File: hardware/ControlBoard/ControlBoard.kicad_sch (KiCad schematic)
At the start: 157 parts, among them J1 Lamp 1 Out, J10 CAN, J11 USB_B_Micro, J12 Conn_01x02, J13 AVAILABLE GPIO, J14 MOTOR_CTRL1, J15 MOTOR_CTRL2, J2 ESTOP1, J3 ESTOP2, J4 Lamp 3 Out, J5 Lamp 2 Out, J6 Lamp 4 Out, J7 PWR_IN, J8 USB_B_Micro, J9 UART BACKUP, Q1 DMN62D0U-13, Q2 DMN62D0U-13, Q3 DMN62D0U-13, Q4 DMN62D0U-13, Q5 SS8050-G, Q6 SS8050-G, SW1 SW_Push, SW2 SW_Push, U1 CP2102N-A02-GQFN28, U2 Lora_Module, U3 AZ1117IH-5.0TRG1, U4 LD1086DT33TR, U5 ESP32-S3-WROOM-1U-N16, U6 74LVC1G97W6-7, U7 SN65HVD232, U8 SN74LVC1GU04DBVR

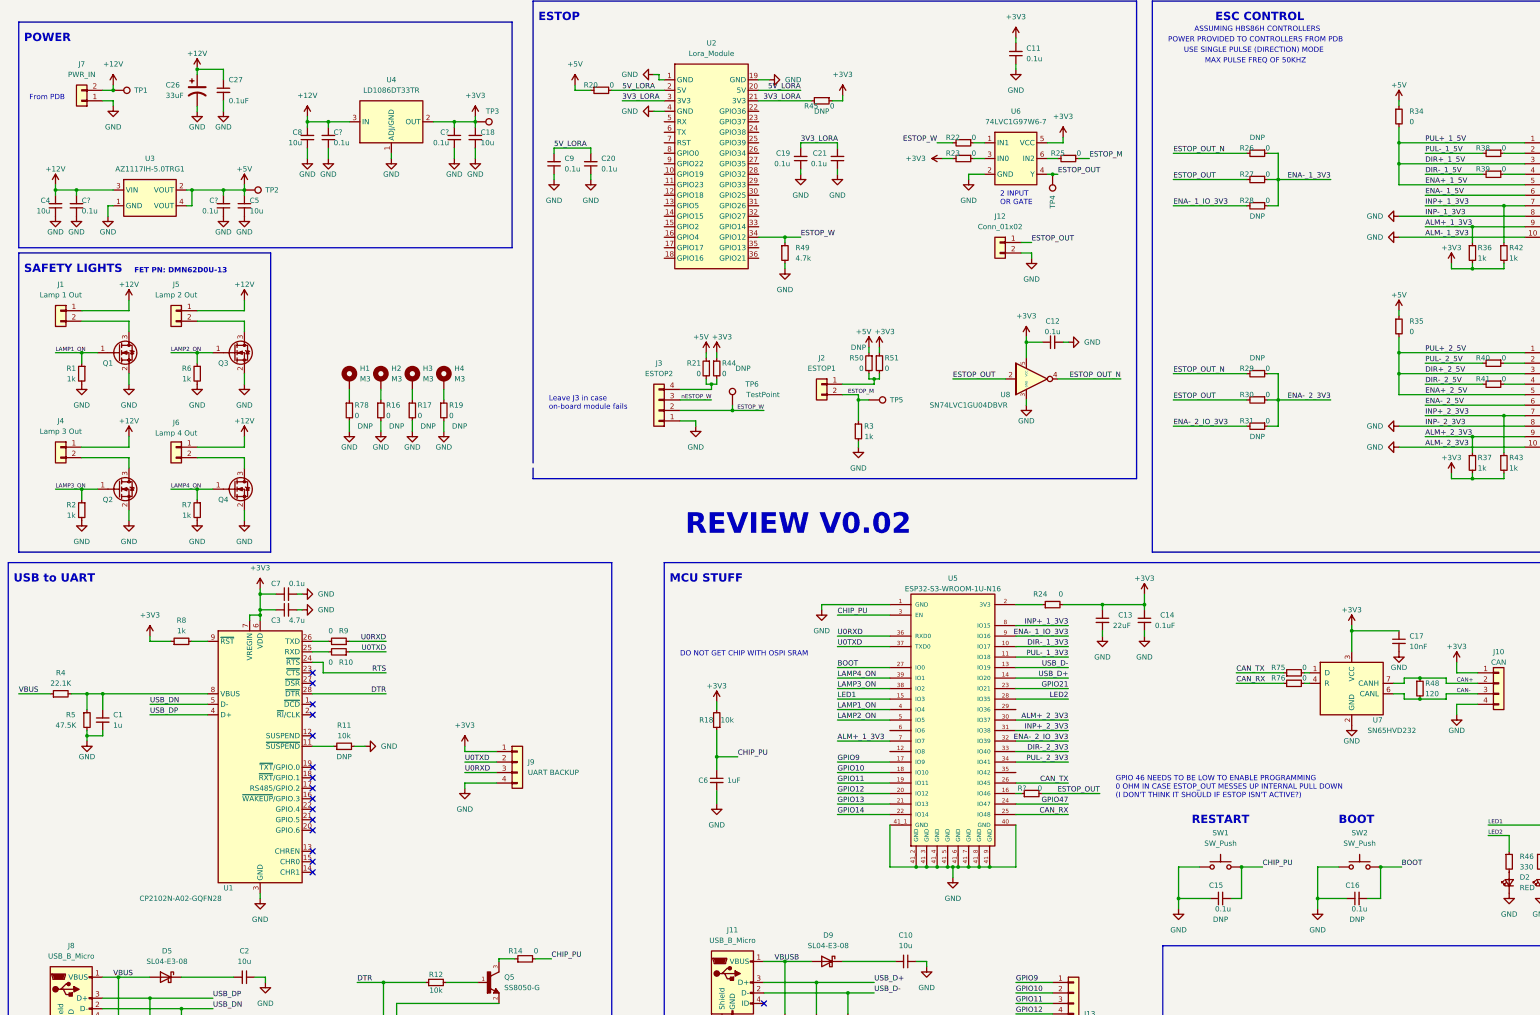
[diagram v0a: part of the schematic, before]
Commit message: Control Board - Replace LDOs, Fix ESP Strapping Pins, W EStop Voltage Divider
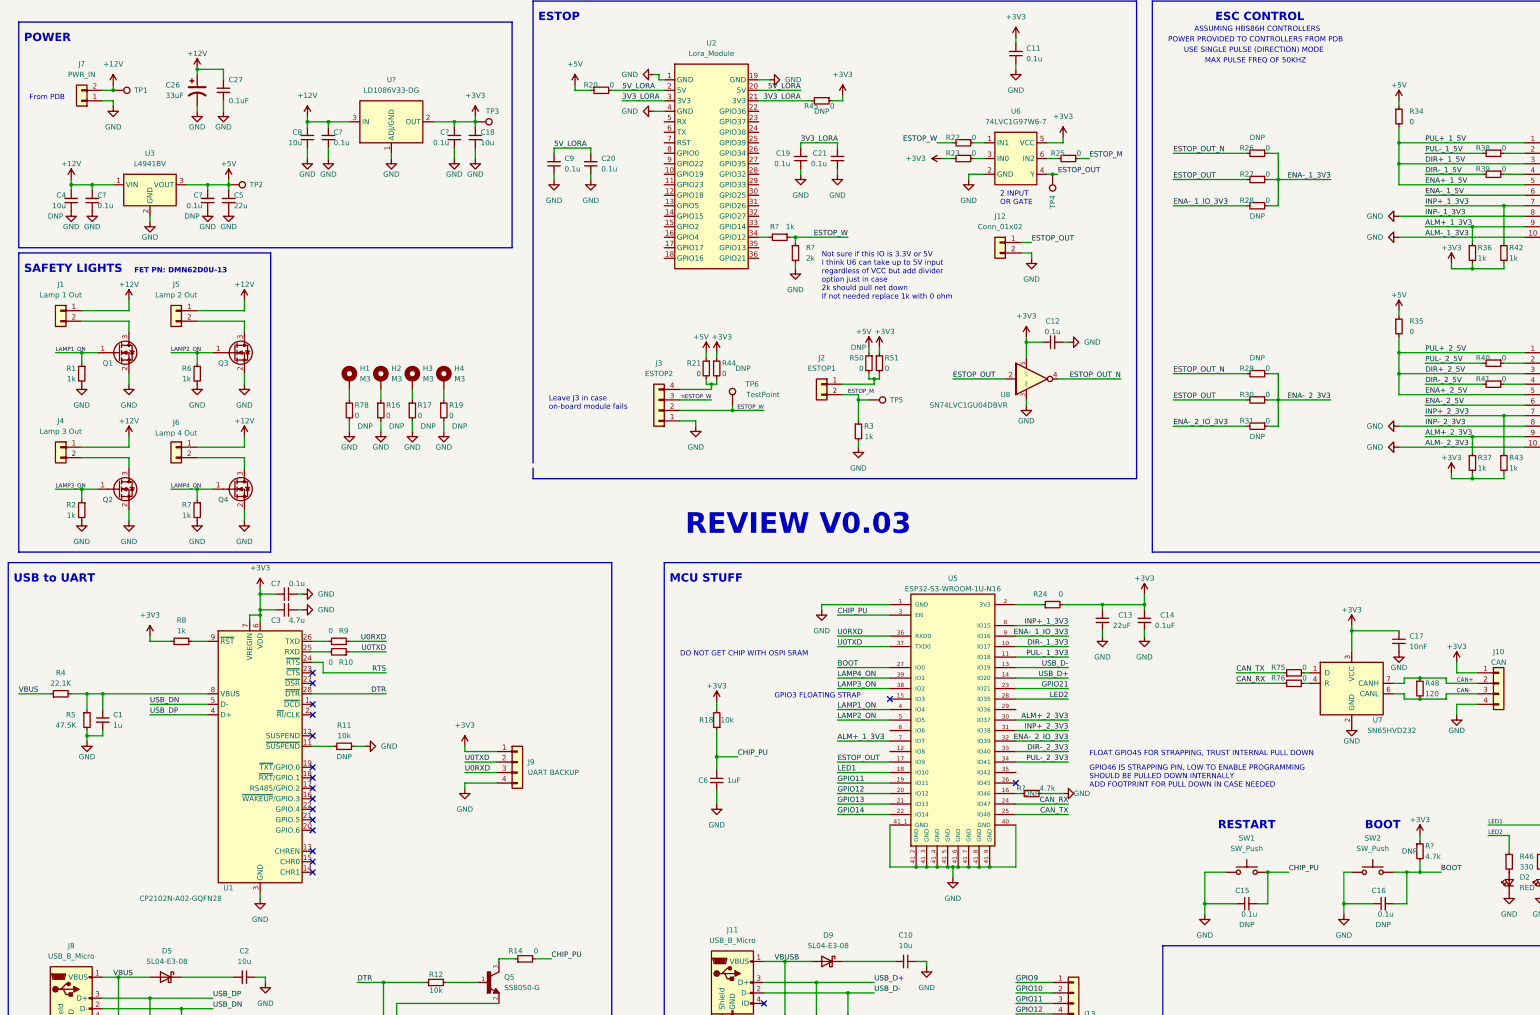
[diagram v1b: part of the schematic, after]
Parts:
- removed R49: 4.7k, Resistor_SMD:R_0805_2012Metric, symbol Device:R_Small
- removed R?: 0, Resistor_SMD:R_0805_2012Metric, symbol Device:R_Small
- removed U3: AZ1117IH-5.0TRG1, controlLib:AZ1117IH-5.0TRG1, symbol controlLib:AZ1117IH-5.0TRG1
- removed U4: LD1086DT33TR, controlLib:LD1086DT33TR, symbol Regulator_Linear:LD1086DT33TR
- added R? (x2): 4.7k, Resistor_SMD:R_0805_2012Metric, symbol Device:R_Small
- added R?: 1k, symbol Device:R_Small
- added R?: 2k, symbol Device:R_Small
- added U3: L4941BV, Package_TO_SOT_THT:TO-220-3_Vertical, symbol controlLib:L4941BV
- added U?: LD1086V33-DG, Package_TO_SOT_THT:TO-220-3_Vertical, symbol Regulator_Linear:LD1086V33-DG
- C4, C?: DNP (none) -> DNP
- C5: value 10u -> 22u
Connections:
- net +12V: now also U3.1 (VIN), U?.3 (IN)
- net +3V3: now also R?.1, U?.2 (OUT)
- net +5V: now also U3.3 (VOUT)
- net BOOT: now also R?.2
- net CAN_RX: now also U5.24 (IO47); no longer U5.25 (IO48)
- net CAN_TX: now also U5.25 (IO48); no longer U5.26 (IO45)
- net ESTOP_OUT: now also U5.17 (IO9)
- net ESTOP_W: now also R?.1, R?.1; no longer U2.34 (GPIO12)
- net GND: now also R?.1, R?.2, U3.2 (GND), U?.1 (ADJ/GND)
- net GPIO10: no longer U5.18 (IO10)
- net GPIO47: no longer U5.24 (IO47)
- net GPIO9: no longer U5.17 (IO9)
- net LED1: now also U5.18 (IO10); no longer U5.15 (IO3)
- net at U5.16 (IO46): now also R?.2
- new net: R?.2, U2.34 (GPIO12)
- no-connect marks 23 -> 25
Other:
- note added: "FLOAT GPIO45 FOR STRAPPING, TRUST INTERNAL PULL DOWN"
- note added: "GPIO3 FLOATING STRAP"
- note added: "GPIO46 IS STRAPPING PIN, LOW TO ENABLE PROGRAMMING SHOULD BE PULLED DOWN INTERNALLY ADD FOOTPRINT FOR PULL DOWN IN CASE NEEDED"
- note added: "Not sure if this IO is 3.3V or 5V I think U6 can take up to 5V input regardless of VCC but add divider option just in case 2k should pull net down If not needed replace 1k with 0 ohm"
- note added: "REVIEW V0.03"
- note removed: "GPIO 46 NEEDS TO BE LOW TO ENABLE PROGRAMMING 0 OHM IN CASE ESTOP_OUT MESSES UP INTERNAL PULL DOWN (I DON'T THINK IT SHOULD IF ESTOP ISN'T ACTIVE?)"
- note removed: "REVIEW V0.02"
- moved on the sheet: C15, C16, C4, C5, C?, SW1, SW2, TP2

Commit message: Most control board schematic fixes done
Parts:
- added C30: 10n, Capacitor_SMD:C_0805_2012Metric, symbol Device:C_Small
- added R32, R33, R49, R52: 220, Resistor_SMD:R_0805_2012Metric, symbol Device:R_Small
- added R57: 4.7k, Resistor_SMD:R_0805_2012Metric, symbol Device:R_Small
- C10, C2: DNP (none) -> DNP; LCSC C92606 -> (none); Voltage (none) -> 5V
- C17: value 10nF -> 0.1u; LCSC C92606 -> (none); Voltage (none) -> 3.3V
- C35, C36: renamed from C?; footprint (none) -> Capacitor_SMD:C_0805_2012Metric
- C6: LCSC C91186 -> (none); Voltage (none) -> 3.3V
- R48: LCSC C269726 -> (none); Power (none) -> 100mW+
- R53, R56: renamed from R?; footprint (none) -> Resistor_SMD:R_0805_2012Metric
- gave numbers to parts that had none: 27
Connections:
- net +3V3: now also C30.2
- net GND: now also C30.1, R57.1
- net LAMP1_ON: now also R32.2; no longer Q1.1 (G)
- net LAMP2_ON: now also R49.2; no longer Q3.1 (G)
- net LAMP3_ON: now also R33.2; no longer Q2.1 (G)
- net LAMP4_ON: now also R52.2; no longer Q4.1 (G)
- net at U5.26 (IO45): now also R57.2
- new net: Q4.1 (G), R52.1
- new net: Q3.1 (G), R49.1
- new net: Q2.1 (G), R33.1
- new net: Q1.1 (G), R32.1
- no-connect marks 25 -> 24
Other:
- note added: "GPIO45 IS PULLED DOWN BY DEFAULT FOR STRAPPING"
- note added: "Lamps are 12V 60mA, FETs dissipate 9mW"
- note added: "REVIEW V0.04"
- note added: "TODO: update this header with remaining open gpio"
- note removed: "FLOAT GPIO45 FOR STRAPPING, TRUST INTERNAL PULL DOWN"
- note removed: "REVIEW V0.03"
- moved on the sheet: C35, C36, J5, J6, Q3, Q4, R1, R2, R6, R7

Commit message: Control Board Rerouting
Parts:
- removed J13: AVAILABLE GPIO, Connector_PinHeader_1.27mm:PinHeader_1x08_P1.27mm_Vertical, symbol Connector_Generic:Conn_01x08
- added J13: Available GPIO, Connector_PinHeader_1.27mm:PinHeader_1x05_P1.27mm_Vertical, symbol Connector_Generic:Conn_01x05
- added R68, R69, R70, R71: 0, Resistor_SMD:R_0805_2012Metric, symbol Device:R_Small
- R65: value 10k -> 0; LCSC C110775 -> C96345
- R67: value 0 -> 10k; LCSC C96345 -> C110775
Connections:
- net +3V3: now also R65.2, R68.2
- net ENA-_1_5V: now also R70.2; no longer J14.6 (Pin_6)
- net ENA-_2_5V: now also R71.2; no longer J15.6 (Pin_6)
- net ESTOP_OUT_N: now also R69.2; no longer R67.2
- net GND: now also R67.2; no longer R65.2
- net GPIO11: now also J13.1 (Pin_1)
- net GPIO12: now also J13.2 (Pin_2)
- net GPIO13: now also J13.3 (Pin_3)
- net GPIO14: now also J13.4 (Pin_4)
- net GPIO21: now also J13.5 (Pin_5)
- net at R61.1, R63.1, U9.8 (OE): now also R65.1
- net at R67.1, U12.8 (OE): now also R68.1, R69.1; no longer R65.1
- new net: J15.6 (Pin_6), R71.1
- new net: J14.6 (Pin_6), R70.1
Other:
- note removed: "TODO: update this header with remaining open gpio"
- moved on the sheet: R63

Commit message: Power Board Schematic Revision Done, Fix Lora Symbol and Update Control Board Routing
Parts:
- removed C20: 0.1u, Capacitor_SMD:C_0805_2012Metric, symbol Device:C_Small
- added R72, R74, R77: 0, Resistor_SMD:R_0805_2012Metric, symbol Device:R_Small
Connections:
- net +3V3: now also R77.1
- net 5V_LORA: no longer U2.20 (5V)
- net GND: now also R72.1, R74.2; no longer U2.1 (GND), U2.19 (GND), U2.4 (GND)
- net 3V3_LORA renamed 3V3_LORA_B
- net 3V3_LORA_B: no longer C19.2, U2.3 (3V3)
- new net: R74.1, U2.19 (GND)
- new net: R72.2, U2.1 (GND)
- new net 3V3_LORA_A: C19.2, R77.2, U2.20 (3V3)
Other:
- note added: "Have seen conflicting pinouts for this online Current pinout matches Amazon picture of what we ordered 0 ohms in case pinout is wrong"
- moved on the sheet: C19, C21, R45

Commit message: Switch 5V LDO for DC DC
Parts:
- removed U3: L4941BV, Package_TO_SOT_THT:TO-220-3_Vertical, symbol controlLib:L4941BV
- added U3: R-78B5.0-2.0, controlLib:R-78B5.0-2.0, symbol controlLib:R-78B5.0-2.0
- C23, C4: DNP DNP -> (none)
- C24, C8: Voltage 12V -> 5V
- C5: value 22u -> 10u
- R38, R39, R40, R41, R70, R71: value 0 -> 1k
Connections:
- net +12V: now also U3.1 (VIN); no longer C24.2, C8.2, U4.3 (IN)
- net +5V: now also C24.2, C8.2, U4.3 (IN), U3.3 (VOUT)
- net GND: now also U3.2 (GND)

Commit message: Last things
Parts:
- added D11: S1G, Diode_SMD:D_SMA, symbol Device:D_Small
- added J16: 5V HEADER, Connector_Molex:Molex_KK-254_AE-6410-03A_1x03_P2.54mm_Vertical, symbol Connector_Generic:Conn_01x03
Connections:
- net +5V: now also D11.1 (K), J16.2 (Pin_2)
- net GND: now also D11.2 (A), J16.3 (Pin_3)
- no-connect marks 24 -> 25
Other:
- moved on the sheet: C18, C24, C25, C8, H1, H2, H3, H4, R16, R17, R19, R78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

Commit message: Finish adding assembly PNs
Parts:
- C1: LCSC C91186 -> C116352
- C11, C17, C22, C23, C24, C25, C28, C29, C32, C33, C35, C36, C38, C39: LCSC (none) -> C519981
- C12: LCSC C1854129 -> C519981
- C14: value 0.1uF -> 0.1u; LCSC C651000 -> C519981; Rating 50V -> 25V
- C18, C5: LCSC (none) -> C237493
- C19, C21, C7, C9: LCSC C651000 -> C519981
- C26: LCSC (none) -> C441625
- C27: value 0.1uF -> 0.1u; LCSC C651000 -> C519981; Voltage (none) -> 12V
- C3: LCSC C90313 -> C87998
- C30: LCSC (none) -> C2688117
- C31, C34, C37, C40, C6: LCSC (none) -> C116352
- C4, C8: LCSC C92606 -> C237493
- D1, D10, D4, D6, D7, D8: LCSC C908199 -> C83324
- D5, D9: DNP (none) -> DNP
- J1, J2, J4, J5, J6: Digikey WM1865-ND -> WM1860-ND; LCSC (none) -> C192562
- J12, J7: LCSC (none) -> C192562
- J16: LCSC (none) -> C471416
- R1, R2, R3, R6, R7: LCSC C280013 -> C510097
- R10, R14, R15, R20, R21, R22, R23, R25, R28, R31, R34, R35, R51, R60, R62, R63, R64, R66, R69, R72, R74, R75, R76, R9: LCSC C96345 -> C237773
- R26, R29: DNP DNP -> (none); LCSC C96345 -> C237773
- R27, R30, R65, R68: DNP (none) -> DNP; LCSC C96345 -> C237773
- R32, R33, R49, R52: LCSC (none) -> C114519
- R36, R37, R42, R43: LCSC C316211 -> C510097
- R38, R39, R40, R41, R70, R71: LCSC C96345 -> C510097
- R4: LCSC C228640 -> C273840
- R44, R45, R50, R77: LCSC (none) -> C237773
- R46, R47: LCSC C229189 -> C105878
- R48: Digikey (none) -> 311-120CRCT-ND; LCSC (none) -> C114245
- R5: LCSC C137519 -> C137519
- R53: DNP (none) -> DNP; LCSC (none) -> C510097
- R54, R55: value 680 -> 1.15k; LCSC C229239 -> C309566
- R56: LCSC (none) -> C127985
- R8: LCSC C110774 -> C510097
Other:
- note added: "MOTOR CONTROLLER LOW VOLTAGE = 0-0.5V, HIGH VOLTAGE = 4-5V MECH SAYS MOTOR SHAFT AT 1120 RPM FOR 5 MPH 1120 RPM -> 3733 HZ DRIVING SIGNAL AT 200 PULSES/REV FILTER IS JUST UNDER 0.5V / JUST OVER 4.5V IDEA IS THAT IT WILL STOP SIGNAL FROM CROSSING THRESHOLD ONCE FREQ GETS TOO HIGH TO PREVENT MOTORS FROM BEING DRIVEN TOO FAST THIS IS MY ATTEMPT AT HARDWARE SPEED CONTROL CAN TINKER WITH THIS ONCE WE 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"
- note removed: "MOTOR CONTROLLER LOW VOLTAGE = 0-0.5V, HIGH VOLTAGE = 4-5V MECH SAYS MOTOR SHAFT AT 940 RPM FOR 5 MPH 940 RPM -> 3133 HZ DRIVING SIGNAL AT 200 PULSES/REV FILTER IS JUST UNDER 0.5V / JUST OVER 4.5V IDEA IS THAT IT WILL STOP SIGNAL FROM CROSSING THRESHOLD ONCE FREQ GETS TO HIGH TO PREVENT MOTORS FROM BEING DRIVEN TOO FAST THIS IS MY ATTEMPT AT HARDWARE SPEED CONTROL CAN TINKER WITH THIS ONCE WE GET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"

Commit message: Build Files
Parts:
- C10, C2: value 10u -> 10u_DNP
- C15, C16: value 0.1u -> 0.1u_DNP
- D5, D9: value SL04-E3-08 -> SL04-E3-08_DNP
- J13: value Available GPIO -> Available GPIO_DNP
- R11: value 10k -> 10k_DNP
- R16, R17, R19, R27, R28, R30, R31, R44, R45, R50, R60, R62, R64, R65, R66, R68, R77, R78: value 0 -> 0_DNP
- R53: value 1k -> 0; DNP DNP -> (none); LCSC C510097 -> C237773
- R57, R58, R59: value 4.7k -> 4.7k_DNP
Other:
- note added: "Not sure if this IO is 3.3V or 5V I think U6 can take up to 5V input regardless of VCC but add divider option just in case 2k should pull net down If needed replace 0 ohm with 1k"
- note removed: "Not sure if this IO is 3.3V or 5V I think U6 can take up to 5V input regardless of VCC but add divider option just in case 2k should pull net down If not needed replace 1k with 0 ohm"
